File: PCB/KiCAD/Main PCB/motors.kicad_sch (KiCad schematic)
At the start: 36 parts, among them M1 Conn_01x02_Pin, M2 Conn_01x02_Pin, M3 Conn_01x02_Pin, M4 Conn_01x02_Pin, U4 LMD18200, U5 LMD18200, U6 LMD18200, U7 LMD18200

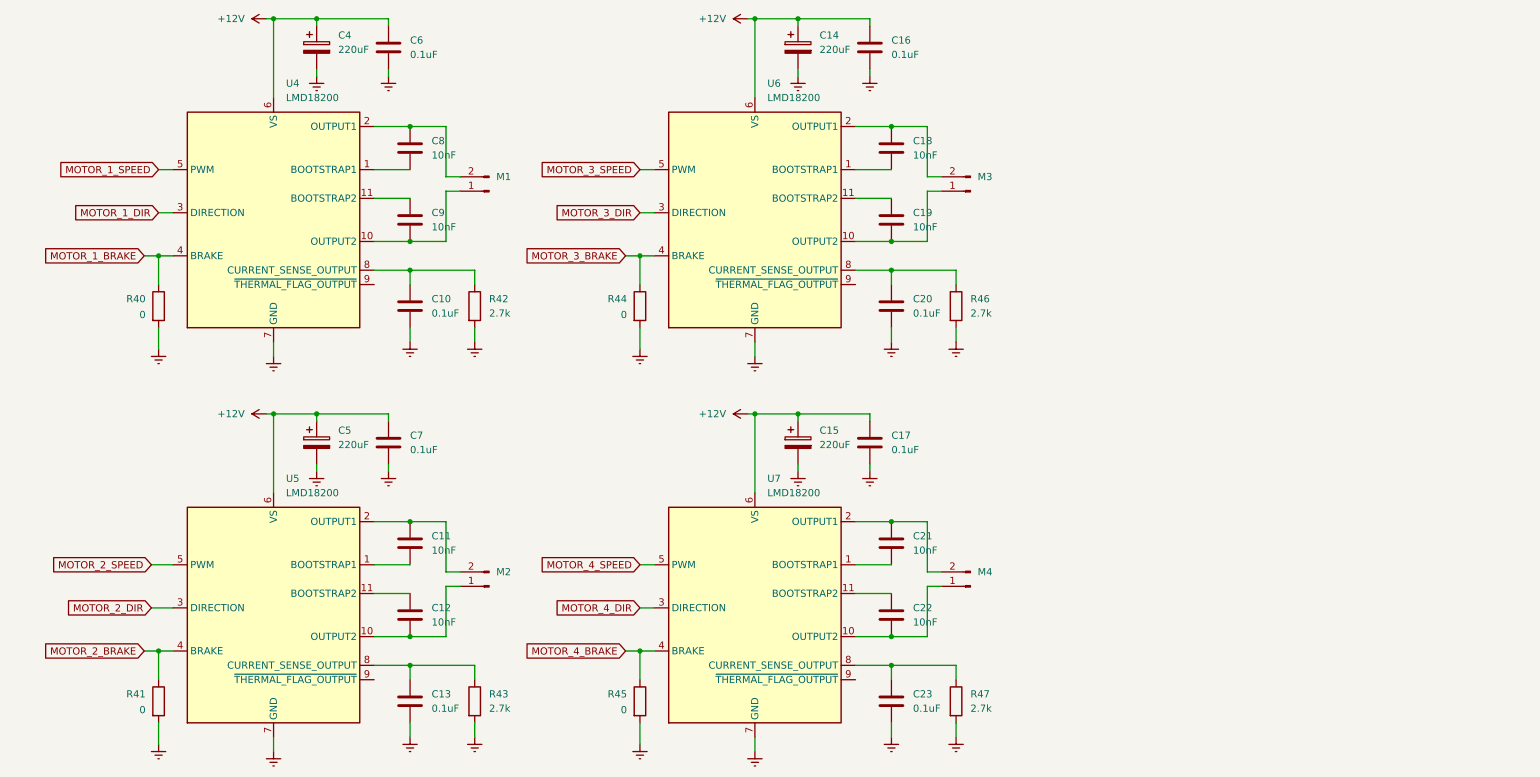
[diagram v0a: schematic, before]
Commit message: New motor controllers for the main PCB
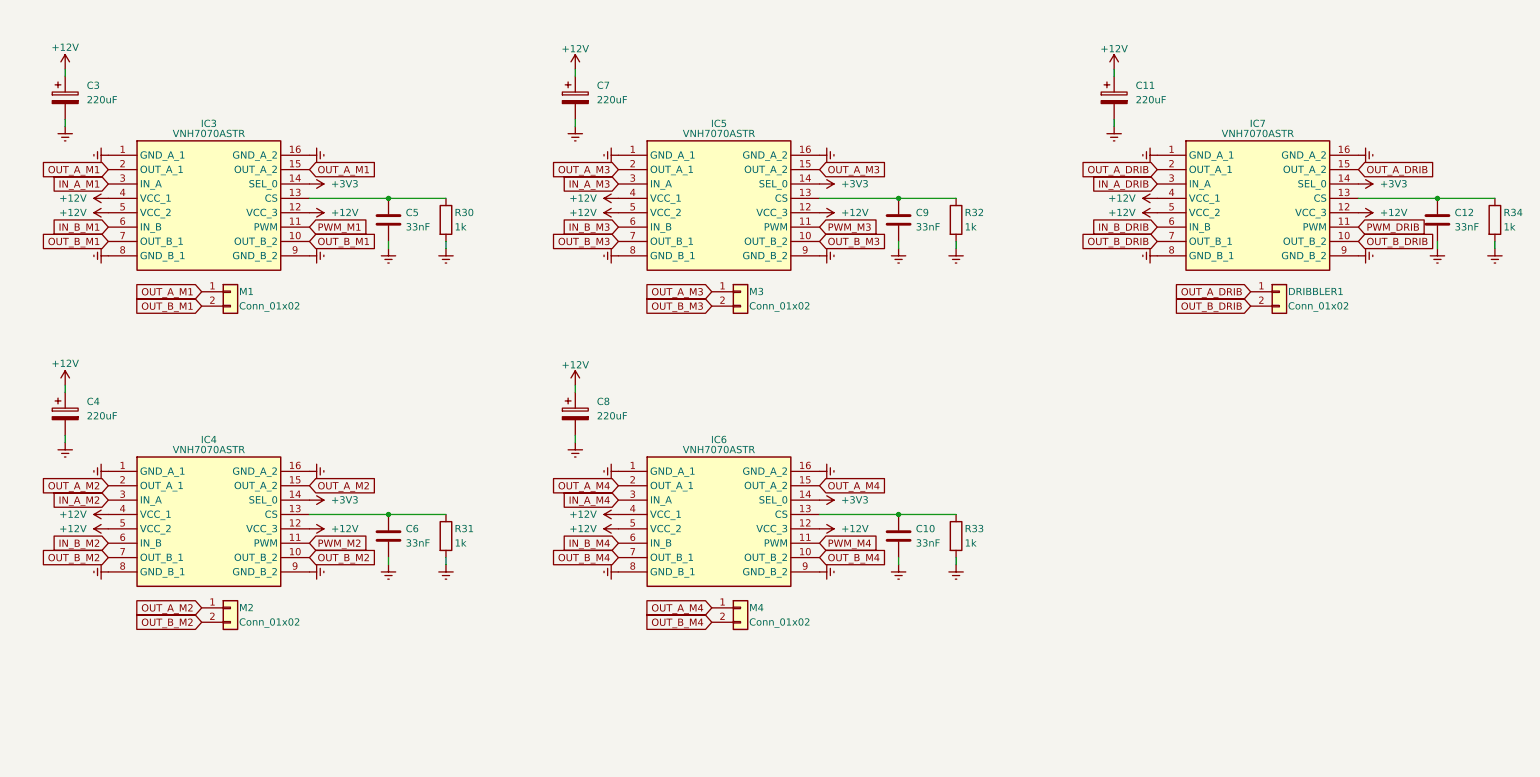
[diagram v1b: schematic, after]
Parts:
- removed C11, C18, C19, C21, C22, C8: 10nF, Capacitor_SMD:C_1210_3225Metric_Pad1.33x2.70mm_HandSolder, symbol Device:C
- removed C13, C16, C17, C20, C23, C7: 0.1uF, Capacitor_SMD:C_0805_2012Metric_Pad1.18x1.45mm_HandSolder, symbol Device:C
- removed C14, C15, C5: 220uF, Capacitor_SMD:CP_Elec_10x10, symbol Device:C_Polarized
- removed M1, M2, M3, M4: Conn_01x02_Pin, Connector_JST:JST_XH_B2B-XH-A_1x02_P2.50mm_Vertical, symbol Connector:Conn_01x02_Pin
- removed R40, R41, R44, R45: 0, Resistor_SMD:R_0805_2012Metric_Pad1.20x1.40mm_HandSolder, symbol Device:R
- removed R43, R46, R47: 2.7k, Resistor_SMD:R_0805_2012Metric_Pad1.20x1.40mm_HandSolder, symbol Device:R
- removed U4, U5, U6, U7: LMD18200, Package_TO_SOT_THT:TO-220-11_P3.4x5.08mm_StaggerOdd_Lead4.58mm_Vertical, symbol Driver_Motor:LMD18200
- added C11, C4, C7, C8: 220uF, Capacitor_SMD:CP_Elec_10x10, symbol Device:C_Polarized
- added C5: 33nF, Capacitor_SMD:C_0805_2012Metric_Pad1.18x1.45mm_HandSolder, symbol Device:C
- added DRIBBLER1, M1, M2, M3, M4: Conn_01x02, Connector_JST:JST_VH_B2P-VH-B_1x02_P3.96mm_Vertical, symbol Connector_Generic:Conn_01x02
- added IC3, IC4, IC5, IC6, IC7: VNH7070ASTR, VNH7070ASTR:SOIC127P600X175-16N, symbol VNH7070ASTR:VNH7070ASTR
- added R31, R32, R33, R34: 1k, Resistor_SMD:R_0805_2012Metric_Pad1.20x1.40mm_HandSolder, symbol Device:R
- C10, C6: value 0.1uF -> 33nF
- C12, C9: value 10nF -> 33nF; footprint Capacitor_SMD:C_1210_3225Metric_Pad1.33x2.70mm_HandSolder -> Capacitor_SMD:C_0805_2012Metric_Pad1.18x1.45mm_HandSolder
- R30: renamed from R42; value 2.7k -> 1k
- renumbered C4 to C3
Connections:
- net +12V: now also C11.1, C4.1, C7.1, C8.1, IC3.12 (VCC_3), IC3.4 (VCC_1), IC3.5 (VCC_2), IC4.12 (VCC_3), IC4.4 (VCC_1), IC4.5 (VCC_2), IC5.12 (VCC_3), IC5.4 (VCC_1), IC5.5 (VCC_2), IC6.12 (VCC_3), IC6.4 (VCC_1), IC6.5 (VCC_2), IC7.12 (VCC_3), IC7.4 (VCC_1), IC7.5 (VCC_2); no longer C6.1
- net GND: now also C12.2, C9.2, C11.2, C4.2, C5.2, C7.2, C8.2, IC3.1 (GND_A_1), IC3.16 (GND_A_2), IC3.8 (GND_B_1), IC3.9 (GND_B_2), IC4.1 (GND_A_1), IC4.16 (GND_A_2), IC4.8 (GND_B_1), IC4.9 (GND_B_2), IC5.1 (GND_A_1), IC5.16 (GND_A_2), IC5.8 (GND_B_1), IC5.9 (GND_B_2), IC6.1 (GND_A_1), IC6.16 (GND_A_2), IC6.8 (GND_B_1), IC6.9 (GND_B_2), IC7.1 (GND_A_1), IC7.16 (GND_A_2), IC7.8 (GND_B_1), IC7.9 (GND_B_2), R31.2, R32.2, R33.2, R34.2
- net at C9.1: now also IC5.13 (CS), R32.1
- net at C10.1: now also IC6.13 (CS), R33.1; no longer R30.1
- net at C12.1: now also IC7.13 (CS), R34.1
- new net: C5.1, IC3.13 (CS), R30.1
- new net: C6.1, IC4.13 (CS), R31.1
- new net +3V3: IC3.14 (SEL_0), IC4.14 (SEL_0), IC5.14 (SEL_0), IC6.14 (SEL_0), IC7.14 (SEL_0)
- new net IN_A_DRIB: IC7.3 (IN_A)
- new net IN_A_M1: IC3.3 (IN_A)
- new net IN_A_M2: IC4.3 (IN_A)
- new net IN_A_M3: IC5.3 (IN_A)
- new net IN_A_M4: IC6.3 (IN_A)
- new net IN_B_DRIB: IC7.6 (IN_B)
- new net IN_B_M1: IC3.6 (IN_B)
- new net IN_B_M2: IC4.6 (IN_B)
- new net IN_B_M3: IC5.6 (IN_B)
- new net IN_B_M4: IC6.6 (IN_B)
- new net OUT_A_DRIB: DRIBBLER1.1 (Pin_1), IC7.15 (OUT_A_2), IC7.2 (OUT_A_1)
- new net OUT_A_M1: IC3.15 (OUT_A_2), IC3.2 (OUT_A_1), M1.1 (Pin_1)
- new net OUT_A_M2: IC4.15 (OUT_A_2), IC4.2 (OUT_A_1), M2.1 (Pin_1)
- new net OUT_A_M3: IC5.15 (OUT_A_2), IC5.2 (OUT_A_1), M3.1 (Pin_1)
- new net OUT_A_M4: IC6.15 (OUT_A_2), IC6.2 (OUT_A_1), M4.1 (Pin_1)
- new net OUT_B_DRIB: DRIBBLER1.2 (Pin_2), IC7.10 (OUT_B_2), IC7.7 (OUT_B_1)
- new net OUT_B_M1: IC3.10 (OUT_B_2), IC3.7 (OUT_B_1), M1.2 (Pin_2)
- new net OUT_B_M2: IC4.10 (OUT_B_2), IC4.7 (OUT_B_1), M2.2 (Pin_2)
- new net OUT_B_M3: IC5.10 (OUT_B_2), IC5.7 (OUT_B_1), M3.2 (Pin_2)
- new net OUT_B_M4: IC6.10 (OUT_B_2), IC6.7 (OUT_B_1), M4.2 (Pin_2)
- new net PWM_DRIB: IC7.11 (PWM)
- new net PWM_M1: IC3.11 (PWM)
- new net PWM_M2: IC4.11 (PWM)
- new net PWM_M3: IC5.11 (PWM)
- new net PWM_M4: IC6.11 (PWM)
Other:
- moved on the sheet: C3, R30

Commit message: Added a BNO055 and traced PCB (incomplete, no DRC pass)
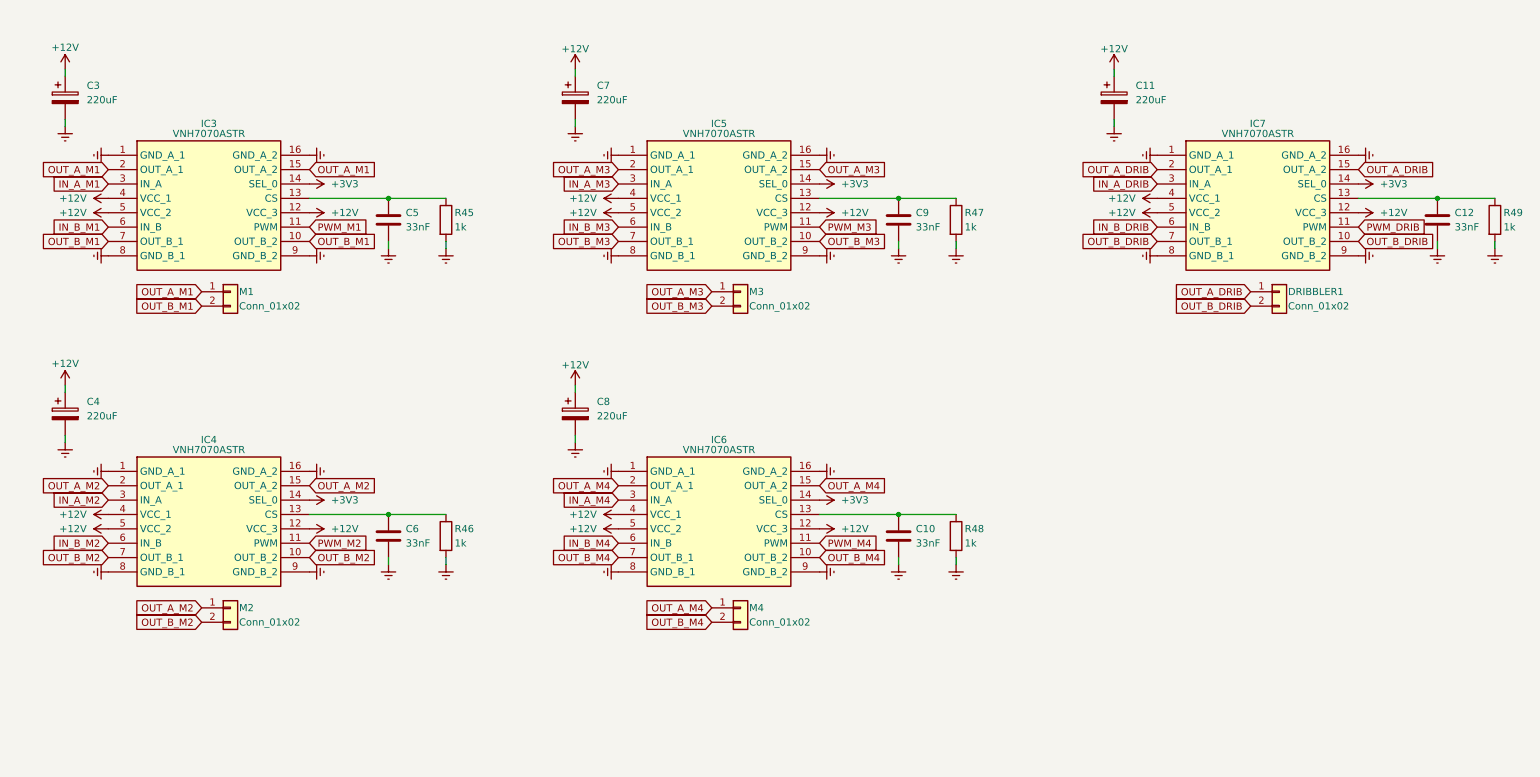
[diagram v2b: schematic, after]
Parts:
- renumbered R30 to R45, R31 to R46, R32 to R47, R33 to R48, R34 to R49

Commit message: Added another switch
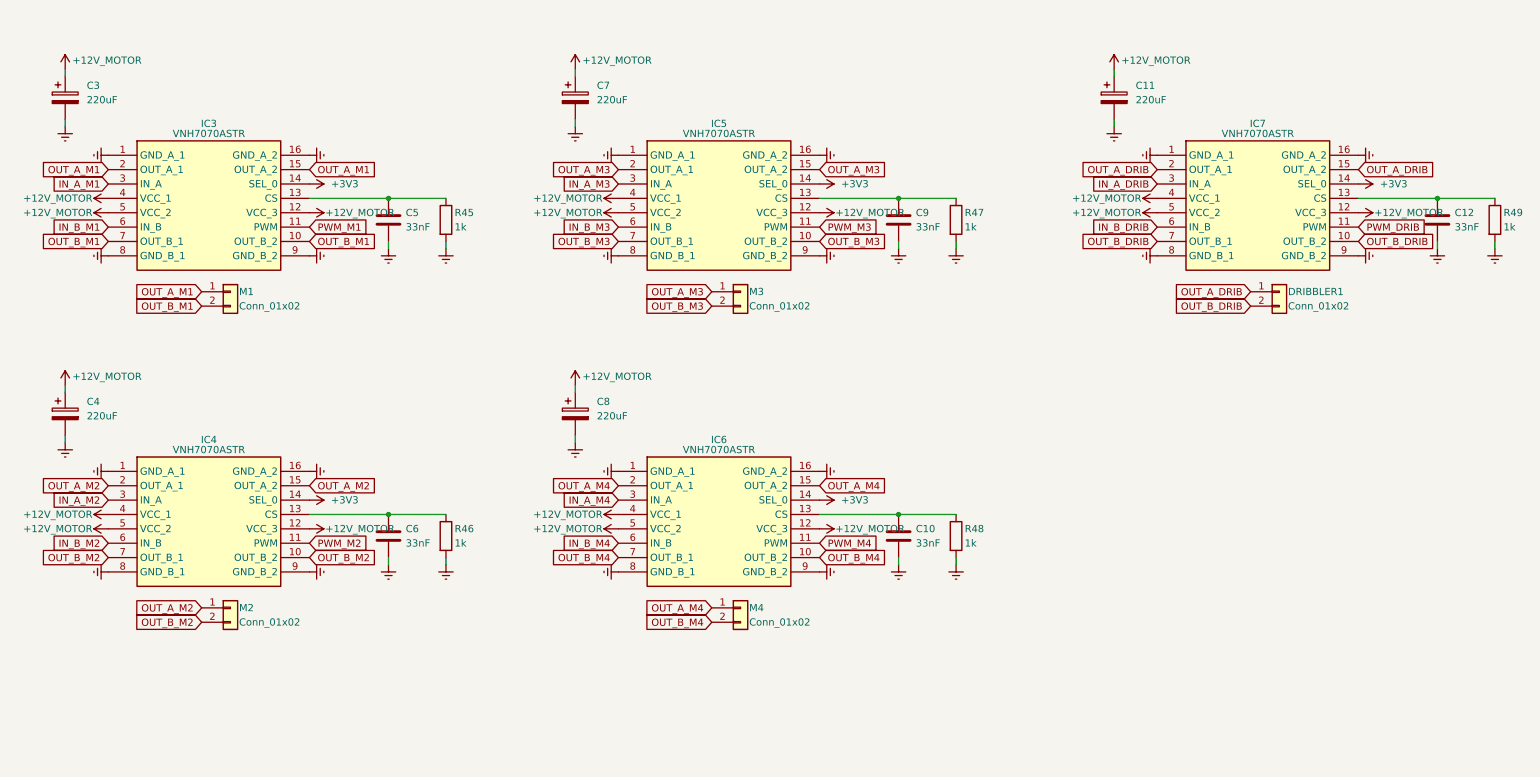
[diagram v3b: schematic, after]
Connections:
- net +12V renamed +12V_MOTOR
